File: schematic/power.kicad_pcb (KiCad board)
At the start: 2 copper layers, 76.7 x 52.7 mm, 14 parts, among them J1 Conn_01x02, J2 Conn_01x02, J3 Conn_01x02, J4 Conn_01x02, J5 Conn_02x06_Odd_Even, J6 Conn_01x02, J7 Conn_01x02, J8 Conn_02x06_Odd_Even, SW1 SW_DIP_x01, U1 LM2595S-3.3

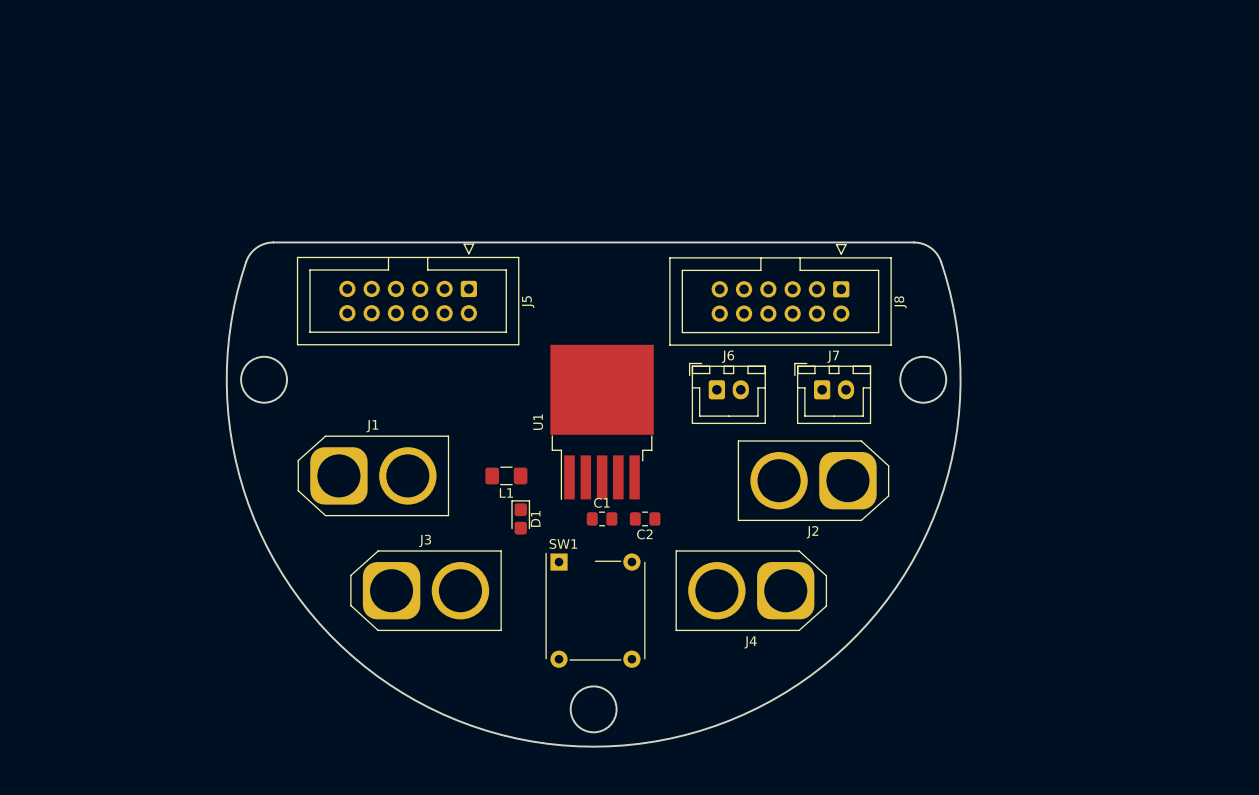
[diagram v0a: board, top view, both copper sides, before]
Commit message: boost converter on Apsu board and PCB design
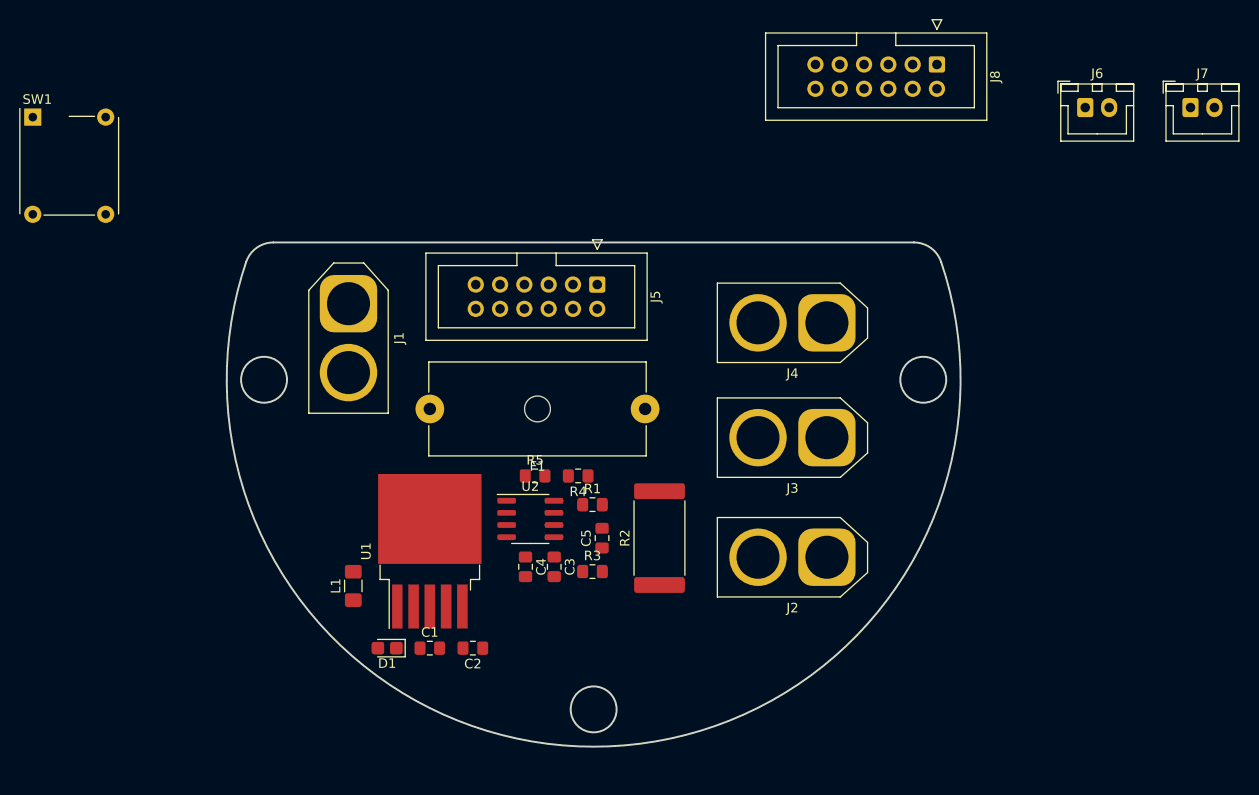
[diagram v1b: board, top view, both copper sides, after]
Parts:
- added C3: 10uF, Capacitor_SMD:C_0805_2012Metric_Pad1.15x1.40mm_HandSolder, F.Cu at (149.0, 114.0)
- added C4: 0.1uF, Capacitor_SMD:C_0805_2012Metric_Pad1.15x1.40mm_HandSolder, F.Cu at (146.0, 114.0)
- added C5: 0.1uF, Capacitor_SMD:C_0805_2012Metric_Pad1.15x1.40mm_HandSolder, F.Cu at (154.0, 111.0)
- added F1: Fuse, Fuse:Fuseholder_Cylinder-5x20mm_Schurter_0031_8201_Horizontal_Open, F.Cu at (158.5, 97.5)
- added R1: 10, Resistor_SMD:R_0805_2012Metric_Pad1.15x1.40mm_HandSolder, F.Cu at (153.0, 107.5)
- added R2: 1m, Resistor_SMD:R_4020_10251Metric_Pad1.65x5.30mm_HandSolder, F.Cu at (160.0, 111.0)
- added R3: 10, Resistor_SMD:R_0805_2012Metric_Pad1.15x1.40mm_HandSolder, F.Cu at (153.0, 114.5)
- added R4: 10k, Resistor_SMD:R_0805_2012Metric_Pad1.15x1.40mm_HandSolder, F.Cu at (151.5, 104.5)
- added R5: 10k, Resistor_SMD:R_0805_2012Metric_Pad1.15x1.40mm_HandSolder, F.Cu at (147.0, 104.5)
- added U2: INA219AxD, Package_SO:SOIC-8_3.9x4.9mm_P1.27mm, F.Cu at (146.5, 109.0)
- moved SW1 72.0 mm to (94.5, 67.0)
- moved J6 48.5 mm to (204.5, 66.0)
- moved J7 48.5 mm to (215.5, 66.0)
- moved J3 48.2 mm to (177.5, 100.5), turned to 180 degrees
- moved J4 28.3 mm to (177.5, 88.5)
- moved J8 25.5 mm to (189.0, 61.5)
- moved C1 22.5 mm to (136.0, 122.5)
- moved C2 22.5 mm to (140.5, 122.5)
- moved U1 22.5 mm to (136.0, 112.4)
- moved L1 19.7 mm to (128.0, 116.0), turned to 90 degrees
- moved D1 19.4 mm to (131.5, 122.5), turned to 180 degrees
- moved J1 18.0 mm to (127.5, 86.5), turned to 270 degrees
- moved J5 13.4 mm to (153.5, 84.5)
- moved J2 8.30 mm to (177.5, 113.0)
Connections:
- J1 pad 2: Net-(J1-Pad2) -> Net-(F1-Pad2)
- SW1 pad 1: Net-(J1-Pad2) -> Net-(C5-Pad1)

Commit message: added extra resistor, removed unnessesary components and added traces to power board
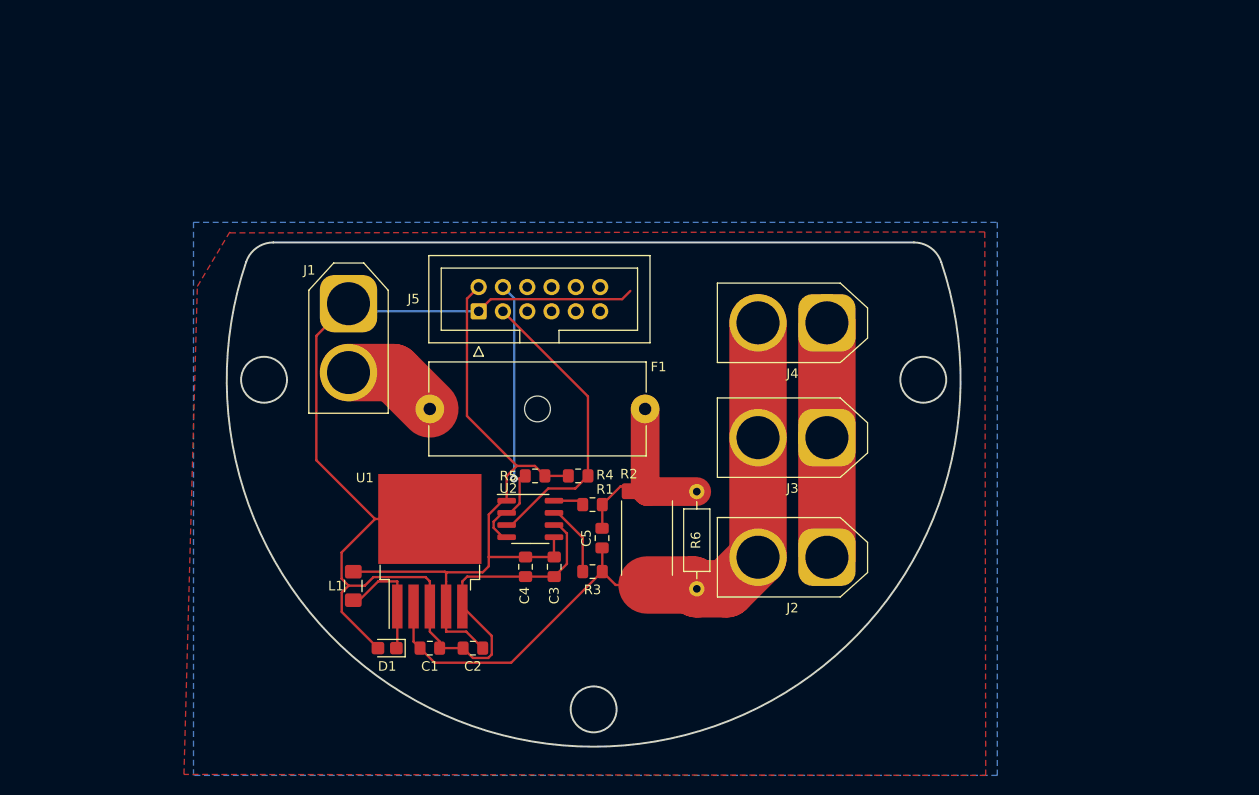
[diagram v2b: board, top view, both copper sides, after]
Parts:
- removed J6, J7: Conn_01x02, Connector_JST:JST_XH_B2B-XH-A_1x02_P2.50mm_Vertical
- removed J8: Conn_02x06_Odd_Even, Connector_IDC:IDC-Header_2x06_P2.54mm_Vertical
- removed SW1: SW_DIP_x01, Button_Switch_THT:SW_MEC_5GTH9
- added R6: R, Resistor_THT:R_Axial_DIN0207_L6.3mm_D2.5mm_P10.16mm_Horizontal, F.Cu at (163.9, 116.3)
- moved J5 12.7 mm to (141.1, 87.3), turned to 90 degrees
- moved R2 1.30 mm to (158.7, 111.0)
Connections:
- C5 pad 1: Net-(C5-Pad1) -> +12V
- R2 pad 1: Net-(C5-Pad1) -> +12V
- R3 pad 2: Net-(C5-Pad1) -> +12V
- U2 pad 1: GND -> +3V3
- U2 pad 2: GND -> I2C-SCL
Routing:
- net GND: track 0.00 -> 152.4 mm
- net +12V: track 0.00 -> 73.6 mm
- net +3V3: track 0.00 -> 73.2 mm
- net I2C-SDA: track 0.00 -> 31.5 mm
- net I2C-SCL: track 0.00 -> 30.3 mm, vias 0 -> 1
- net Net-(C5-Pad2): track 0.00 -> 21.6 mm
- net Net-(D1-Pad1): track 0.00 -> 12.4 mm
- net Net-(F1-Pad2): track 0.00 -> 10.1 mm
- net Net-(R3-Pad1): track 0.00 -> 7.62 mm
- net Net-(R1-Pad1): track 0.00 -> 3.17 mm
- added copper zone on B.Cu, net GND
- added copper zone on F.Cu, net GND
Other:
- board text added: "Aruna power github.com/aruna"

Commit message: power documentation
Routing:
- net GND: track 152.4 -> 138.0 mm
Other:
- board text added: "12V in"
- board text added: "12V out"
- board text added: "GND 12V"
- board text added: "GND V12"
- board text added: "SPI-SS1 SPI-MISO SPI-MOSI RS485-A I²C-SDA GND"
- board text added: "SPI-SS2 SPI-SS0 SPI-SCLK RS485-B I²C-SCL +3V3"
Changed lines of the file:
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@@
   (general
     (thickness 1.6)
-    (drawings 8)
+    (drawings 16)
     (tracks 125)
     (zones 0)
@@
   (page A4)
   (layers
-    (0 F.Cu signal hide)
+    (0 F.Cu signal)
     (31 B.Cu signal hide)
     (32 B.Adhes user)
-    (33 F.Adhes user hide)
-    (34 B.Paste user)
+    (33 F.Adhes user)
+    (34 B.Paste user hide)
     (35 F.Paste user hide)
-    (36 B.SilkS user)
-    (37 F.SilkS user hide)
+    (36 B.SilkS user hide)
+    (37 F.SilkS user)
     (38 B.Mask user)
     (39 F.Mask user hide)
@@
     )
   )
+  (gr_text "GND      V12" (at 173.9 107.9) (layer B.SilkS)
+    (effects (font (size 1 1) (thickness 0.15)) (justify mirror))
+  )
+  (gr_text "GND      V12" (at 173.8 95.3) (layer B.SilkS)
+    (effects (font (size 1 1) (thickness 0.15)) (justify mirror))
+  )
+  (gr_text "GND      V12" (at 174 83.2) (layer B.SilkS)
+    (effects (font (size 1 1) (thickness 0.15)) (justify mirror))
+  )
+  (gr_text "GND\n\n\n\n12V" (at 134 90.5) (layer B.SilkS)
+    (effects (font (size 1 1) (thickness 0.15)) (justify mirror))
+  )
+  (gr_text "12V out" (at 173.3 82.6) (layer F.SilkS)
+    (effects (font (size 1 1) (thickness 0.15)))
+  )
+  (gr_text "12V in" (at 127.4 99.9) (layer F.SilkS)
+    (effects (font (size 1 1) (thickness 0.15)))
+  )
+  (gr_text "SPI-SS1\nSPI-MISO\nSPI-MOSI\nRS485-A\nI²C-SDA\nGND" (at 159.1 86.3 270) (layer B.SilkS)
+    (effects (font (size 0.5 0.5) (thickness 0.125)) (justify right mirror))
+  )
+  (gr_text "SPI-SS2\nSPI-SS0\nSPI-SCLK\nRS485-B\nI²C-SCL\n+3V3" (at 159.1 85.7 270) (layer B.SilkS)
+    (effects (font (size 0.5 0.5) (thickness 0.125)) (justify left mirror))
+  )
   (gr_text "Aruna power\ngithub.com/aruna" (at 153 123.1) (layer B.SilkS)
     (effects (font (size 1 1) (thickness 0.15)) (justify mirror))
@@
   (gr_line (start 186.6 80.1) (end 119.643298 80.1) (layer Edge.Cuts) (width 0.2))
   (segment (start 130.2747 109) (end 124.1372 102.8625) (width 0.25) (layer F.Cu) (net 1))
-  (segment (start 124.1372 102.8625) (end 124.1372 89.8628) (width 0.25) (layer F.Cu) (net 1))
-  (segment (start 124.1372 89.8628) (end 127.5 86.5) (width 0.25) (layer F.Cu) (net 1))
   (segment (start 130.2747 109) (end 126.7781 112.4966) (width 0.25) (layer F.Cu) (net 1))
   (segment (start 126.7781 112.4966) (end 126.7781 115.2423) (width 0.25) (layer F.Cu) (net 1))
@@
   (segment (start 128.3 87.3) (end 127.5 86.5) (width 0.25) (layer B.Cu) (net 1))
   (segment (start 136 119.35) (end 136 120.7753) (width 0.25) (layer F.Cu) (net 1))
-  (segment (start 139.4 118.15) (end 142.4705 121.2205) (width 0.25) (layer F.Cu) (net 1))
-  (segment (start 142.4705 121.2205) (end 142.4705 123.1624) (width 0.25) (layer F.Cu) (net 1))
   (segment (start 142.4705 123.1624) (end 142.1065 123.5264) (width 0.25) (layer F.Cu) (net 1))
   (segment (start 142.1065 123.5264) (end 140.5014 123.5264) (width 0.25) (layer F.Cu) (net 1))
@@
   (segment (start 139.475 122.5) (end 137.025 122.5) (width 0.25) (layer F.Cu) (net 1))
   (segment (start 177.5 100.5) (end 177.5 113) (width 6) (layer F.Cu) (net 1))
+  (segment (start 142.4705 123.1624) (end 142.4705 123.1295) (width 0.25) (layer F.Cu) (net 1))
+  (segment (start 146 119.541) (end 146 115.025) (width 0.25) (layer F.Cu) (net 1))
+  (segment (start 142.4705 123.0705) (end 146 119.541) (width 0.25) (layer F.Cu) (net 1))
+  (segment (start 142.4705 123.1624) (end 142.4705 123.0705) (width 0.25) (layer F.Cu) (net 1))
   (segment (start 145.0947 103.4536) (end 146.9786 103.4536) (width 0.25) (layer F.Cu) (net 2))
   (segment (start 146.9786 103.4536) (end 148.025 104.5) (width 0.25) (layer F.Cu) (net 2))
